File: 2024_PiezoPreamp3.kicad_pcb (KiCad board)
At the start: 4 copper layers, 71 x 36.8 mm, 91 parts, among them J101 6.3mm stereo, J102 6.3mm stereo, J201 DC IN 5.5/2.1mm, J401 Spring Contact, U101 OPA145, U102 OPA145, U201 ZXMP3A17E6TA, U301 BC847BS,115

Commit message: Schematic, PCB: moving DC ESD protection in front of the switch. Using one 22uF bulk decoupling cap where DC enters the board instead of two 10uF near opamps. Using 22uF instead of 10uF in opamp biasing to remove 10uF from BOM completely
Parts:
- removed the C203 at (158.9, 91.7)
- removed the C205 at (162.4, 83.0)
- removed C207: 10u, library:cap_CL21A106KAYNNNE
- added C201: 22u, library:cap_CL31A226KAHNNNE, F.Cu at (184.3, 83.5)
- added C204: 22u, library:cap_CL31A226KAHNNNE, F.Cu at (158.7, 91.2)
- moved D201 17.0 mm to (184.3, 88.2), turned to 90 degrees
- renumbered C201 to C202, C202 to C203, C204 to C205
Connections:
- D201 pad 2: /2-Power/DC_IN_ESD -> /2-Power/DC_IN_POS
- S201 pad 11: /2-Power/DC_IN_ESD -> /2-Power/RP_DRAIN
- U201 pad 1: /2-Power/DC_IN_ESD -> /2-Power/RP_DRAIN
- U201 pad 2: /2-Power/DC_IN_ESD -> /2-Power/RP_DRAIN
- U201 pad 5: /2-Power/DC_IN_ESD -> /2-Power/RP_DRAIN
- U201 pad 6: /2-Power/DC_IN_ESD -> /2-Power/RP_DRAIN
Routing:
- net /2-Power/DC_IN_ESD: track 30.3 -> 0.00 mm
- net /2-Power/RP_DRAIN: track 0.00 -> 22.8 mm
- net Vbias: track 24.8 -> 15.9 mm
- net GND: track 10.4 -> 9.11 mm, vias 27 -> 26
- net VS: track 53.3 -> 52.2 mm

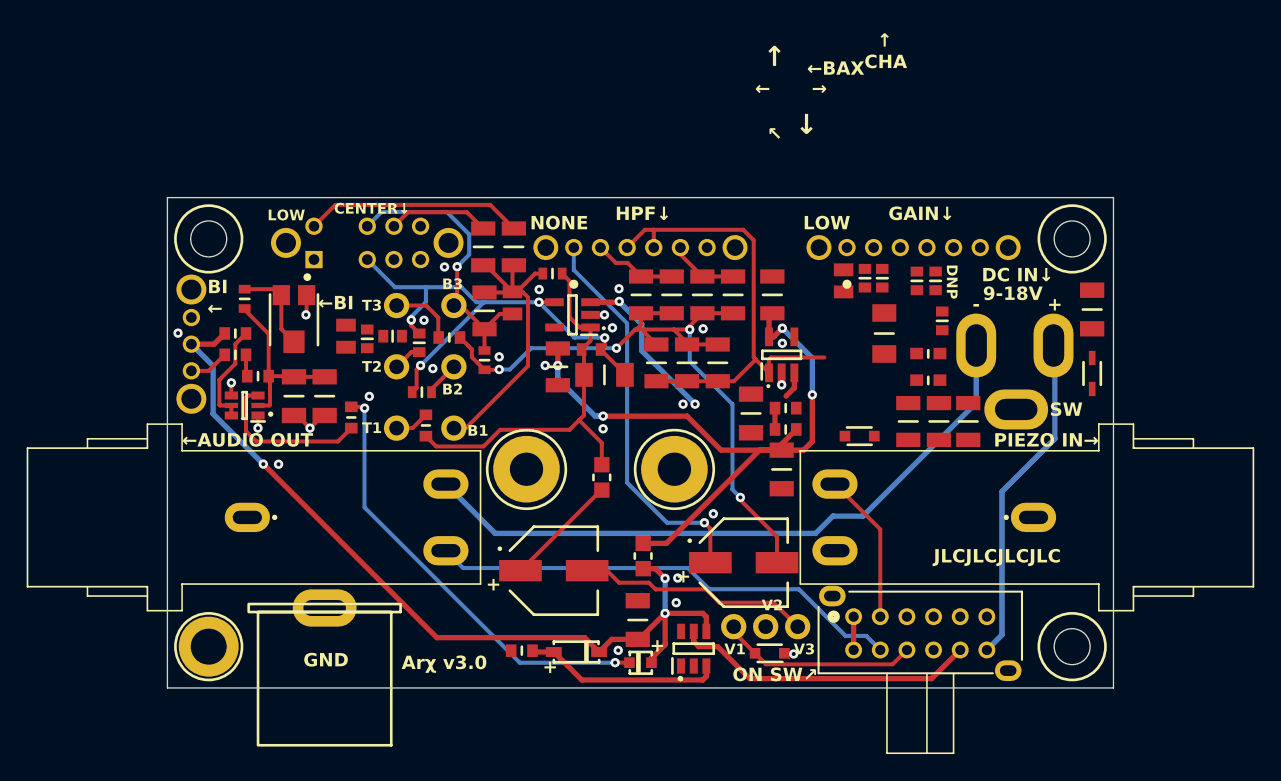
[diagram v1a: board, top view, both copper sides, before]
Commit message: PCB: changing power traces to 0.5mm width again. I have enough space and the inductance is lower
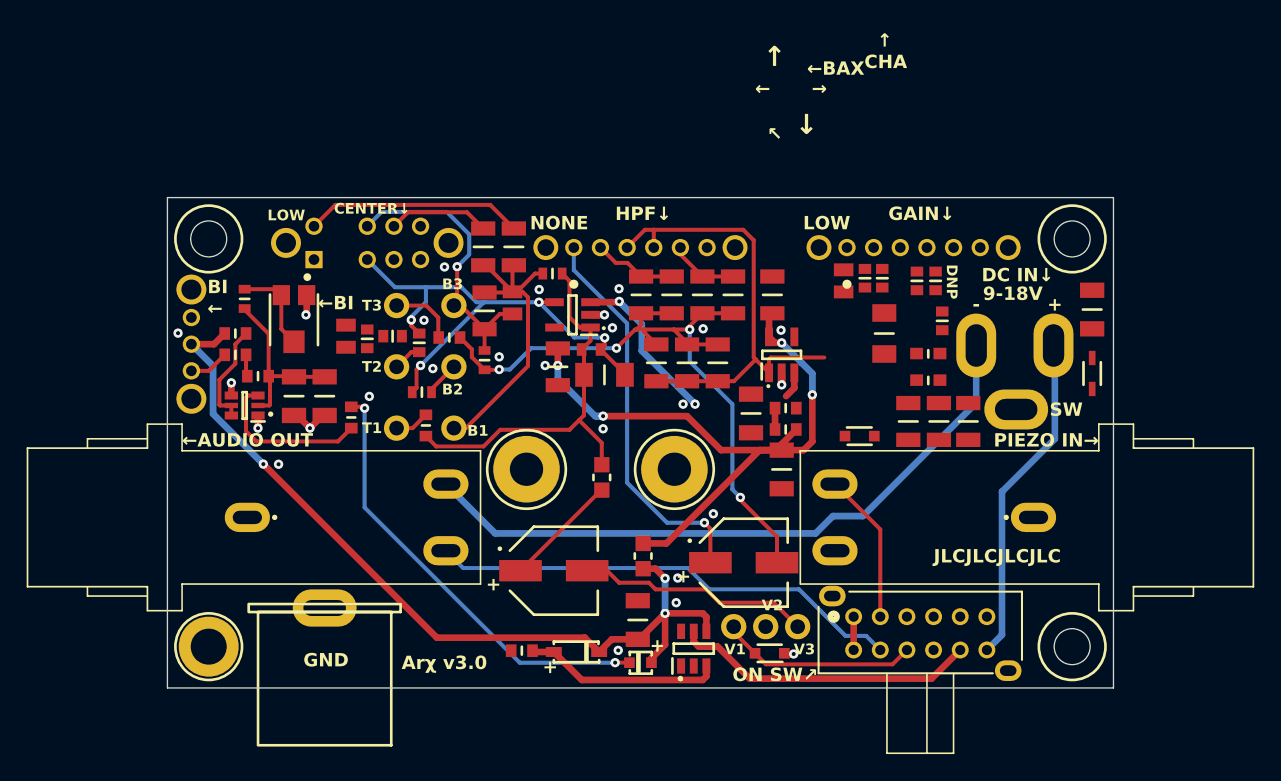
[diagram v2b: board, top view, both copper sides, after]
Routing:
- net VS: track 52.2 -> 51.0 mm

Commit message: PCB: enlarging all the pads that will be manually soldered
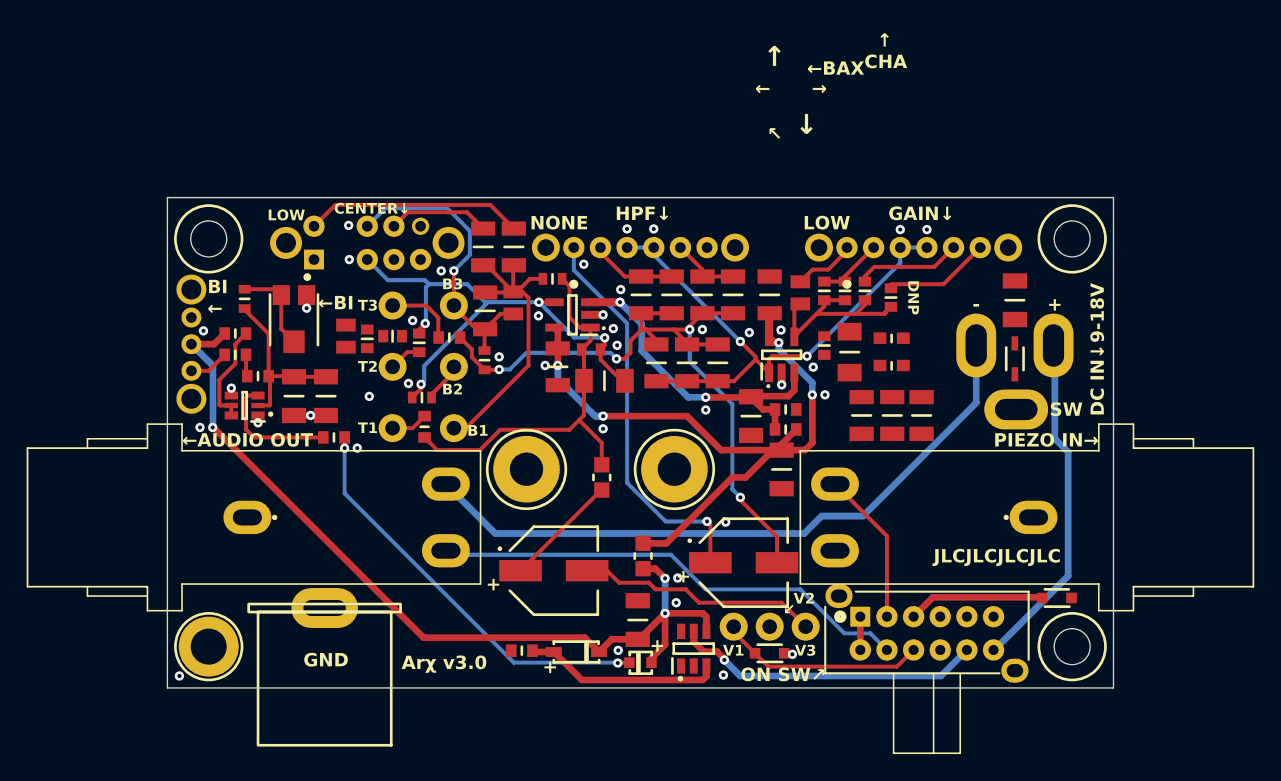
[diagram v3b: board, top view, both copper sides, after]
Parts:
- D202: value DDZ12B-7 -> SOD3716X145N
- S201: value EG4208A -> SWITCH12_EG4208A_EWI
- U201: value ZXMP3A17E6TA -> SOT95P285X140-6N
- moved D101 19.1 mm to (181.7, 105.1), turned to 180 degrees
- moved Cf101 9.04 mm to (164.2, 86.2)
- moved D201 5.90 mm to (178.5, 87.2)
- moved C201 5.84 mm to (178.5, 82.8)
- moved Cf105 3.97 mm to (167.2, 82.0)
- moved Cf106 3.58 mm to (169.2, 82.5)
- moved C101 3.53 mm to (169.3, 91.4)
- moved C102 3.53 mm to (171.5, 91.4)
- moved C103 3.53 mm to (167.0, 91.4)
- moved Cf102 3.37 mm to (162.4, 82.2)
- moved Cf104 3.19 mm to (164.2, 82.0)
- moved R101 2.98 mm to (169.2, 85.6)
- moved R102 2.96 mm to (169.2, 87.7)
- moved Cf103 2.96 mm to (165.8, 82.0)
- moved Rf101 2.95 mm to (166.1, 86.7)
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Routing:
- net /1-ChargeAmpAndEQ/CH_A_INV: track 0.00 -> 14.7 mm
- net PIEZO_ESD: track 0.00 -> 10.3 mm
- net Vbias: track 15.9 -> 24.7 mm
- net /1-ChargeAmpAndEQ/G_SW_5: track 0.00 -> 7.94 mm
- net /1-ChargeAmpAndEQ/G_SW_6: track 0.00 -> 7.84 mm
- net /1-ChargeAmpAndEQ/G_SW_1: track 0.00 -> 5.06 mm
- net /1-ChargeAmpAndEQ/G_SW_2: track 0.00 -> 4.96 mm
- net /1-ChargeAmpAndEQ/CH_A_OUT: track 35.5 -> 40.1 mm, vias 0 -> 3
- net /3-BatteryIndicator/BI_C2: track 12.1 -> 9.41 mm
- net /3-BatteryIndicator/LED_K: track 33.2 -> 30.9 mm
- net GND: track 9.11 -> 6.89 mm, vias 26 -> 39
- net VS: track 51.0 -> 52.6 mm
- net /1-ChargeAmpAndEQ/BAX_IN: track 53.0 -> 54.2 mm
- net /1-ChargeAmpAndEQ/BAX_A_INV: track 38.4 -> 39.4 mm
- net /2-Power/DC_IN_POS: track 25.0 -> 25.7 mm
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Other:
- board text added: "↙"

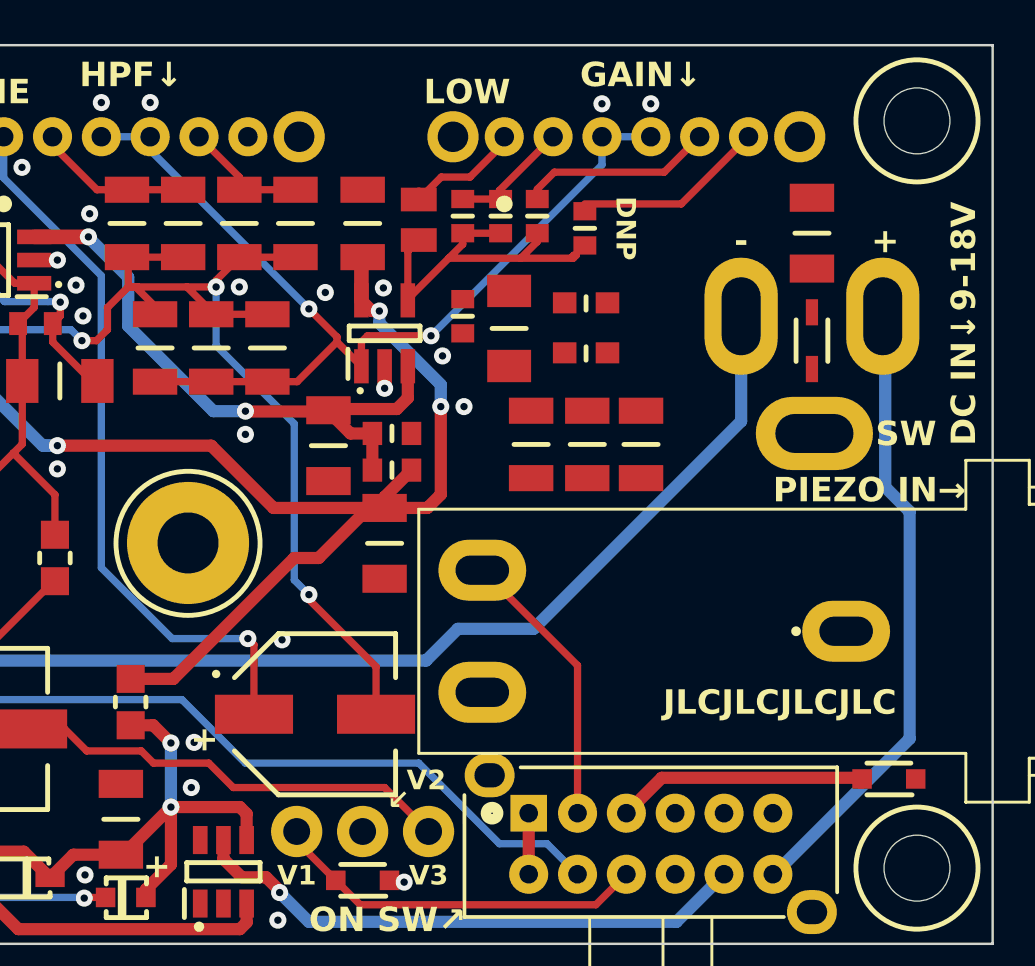
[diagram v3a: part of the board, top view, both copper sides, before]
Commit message: Using larger footprint for DNP feedback cap; small improvements
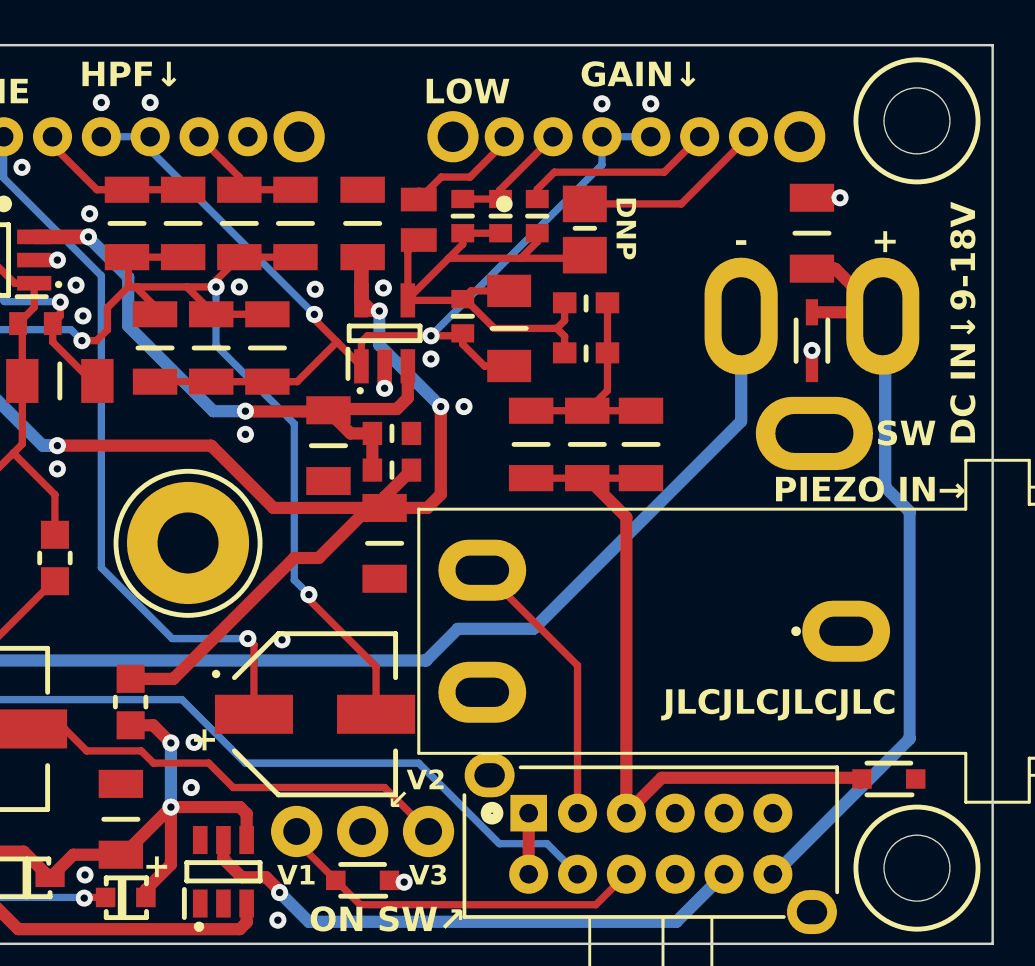
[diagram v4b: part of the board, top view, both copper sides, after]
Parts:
- Cf106: footprint library:GRM1885C1H102JA01D -> library:cap_SMD_DNP
- D202: value SOD3716X145N -> DDZ12B-7
- S201: value SWITCH12_EG4208A_EWI -> EG4208A
- U201: value SOT95P285X140-6N -> ZXMP3A17E6TA
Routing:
- net PIEZO_ESD: track 10.3 -> 29.2 mm
- net /1-ChargeAmpAndEQ/CH_A_INV: track 14.7 -> 25.6 mm
- net /1-ChargeAmpAndEQ/CIN_RIN: track 0.00 -> 9.26 mm
- net /2-Power/DC_IN_POS: track 25.7 -> 32.3 mm
- net /1-ChargeAmpAndEQ/CH_A_OUT: track 40.1 -> 44.2 mm, vias 3 -> 2
- net GND: track 6.89 -> 8.80 mm, vias 39 -> 42

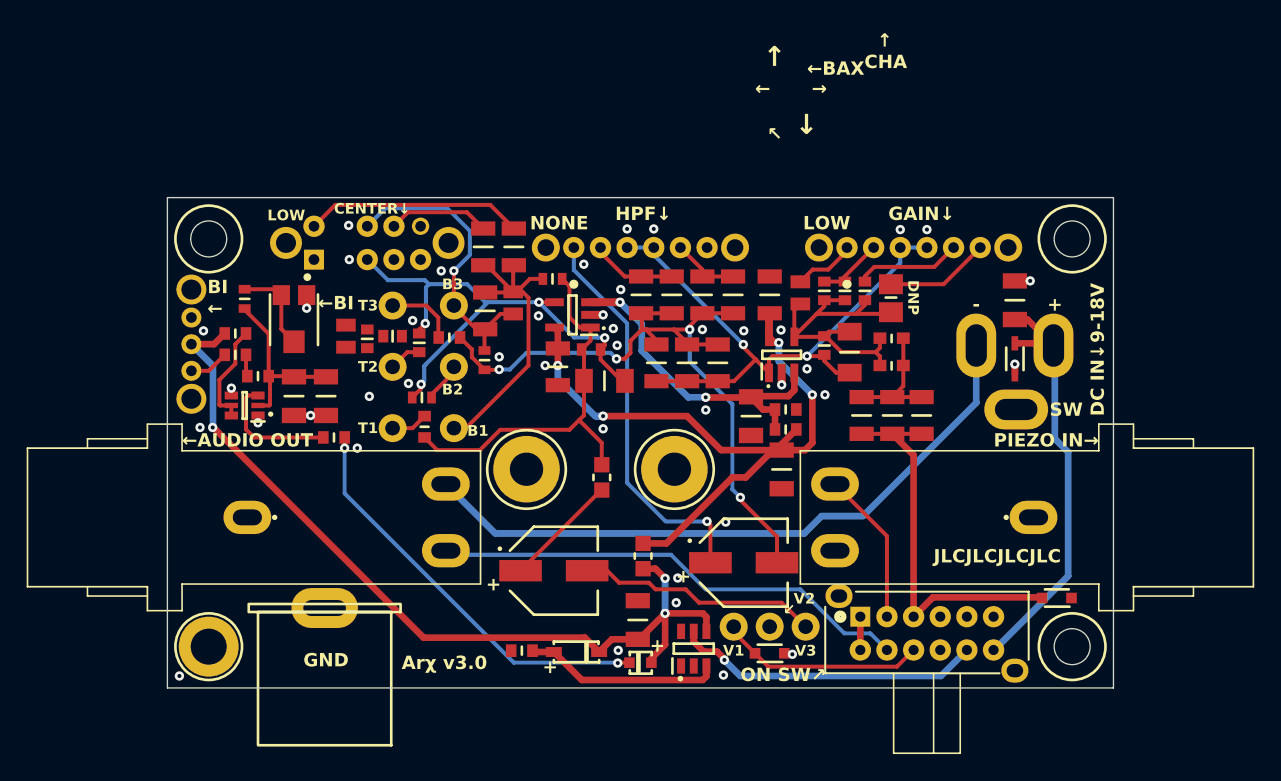
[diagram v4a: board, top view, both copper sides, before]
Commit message: PCB: finishing layout & routing, improving silkscreen everywhere, checking rules
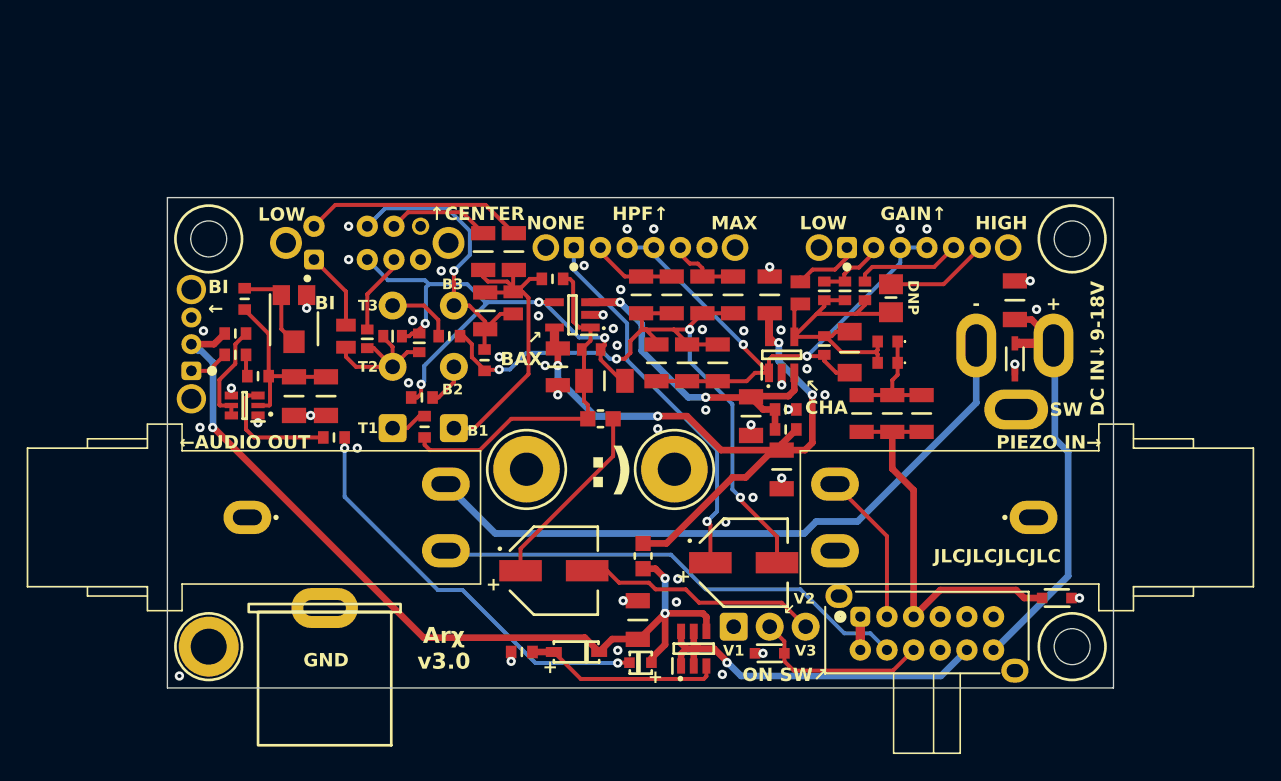
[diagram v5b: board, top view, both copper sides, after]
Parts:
- C205, C206, Cb103, Chp107: footprint library:GRM31C5C2A104JA01L -> library:GRM31C5C1H104JA01L
- H101, H104, H107: footprint library:FreePad_1.1mm_2.0mm -> library:FreePad_1.1mm_2.1mm_rect
- H102, H103, H105, H106, H108, H109: footprint library:FreePad_1.1mm_2.0mm -> library:FreePad_1.1mm_2.1mm
- R101, R102: footprint library:RT0603BRE07150RL_UL-M -> library:ERA-3AEB151V
- R103, R303, Rb101, Rb102: footprint library:ERA-3AEB392V -> library:RT0603FRE073K9L
- R203, R204, R301, R302, R304: footprint library:RT0603BRD0747KL -> library:RT0603FRD0747KL
- moved R105 4.40 mm to (147.4, 91.7), turned to 180 degrees
- moved H107 2.70 mm to (157.4, 107.2)
- moved H108 2.70 mm to (160.1, 107.2)
- moved R101 0.39 mm to (168.9, 85.8)
- moved R102 0.36 mm to (168.9, 87.5)
- moved Cb103 0.35 mm to (140.9, 79.1)
- moved Cb104 0.35 mm to (138.6, 79.1)
- moved C101 0.15 mm to (169.3, 91.2)
- moved C102 0.15 mm to (171.5, 91.2)
- moved C103 0.15 mm to (167.0, 91.2)
- moved R201 0.10 mm to (141.5, 109.2)
- moved Rt101 0.10 mm to (136.1, 85.5)
- turned D102 to 0 degrees
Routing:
- net /1-ChargeAmpAndEQ/TREB_2: track 2.46 -> 12.1 mm
- net GND: track 8.80 -> 15.2 mm, vias 42 -> 51
- net /1-ChargeAmpAndEQ/C_SW_2: track 0.00 -> 6.08 mm
- net /1-ChargeAmpAndEQ/C_SW_1: track 0.00 -> 5.91 mm
- net /1-ChargeAmpAndEQ/ROUT_COUT: track 8.61 -> 14.3 mm
- net /2-Power/RP_DRAIN: track 23.3 -> 28.9 mm
- net VS: track 52.6 -> 56.3 mm
- net /1-ChargeAmpAndEQ/BAX_A_OUT: track 29.4 -> 27.1 mm
- net AUDIO_ESD: track 15.5 -> 13.7 mm
- net /1-ChargeAmpAndEQ/BAX_A_INV: track 39.4 -> 41.0 mm
- net /1-ChargeAmpAndEQ/HPF_SW_1: track 29.7 -> 28.5 mm
- net /1-ChargeAmpAndEQ/BASS_1: track 23.8 -> 24.7 mm
- net /1-ChargeAmpAndEQ/CH_A_INV: track 25.6 -> 25.0 mm
- net PIEZO_ESD: track 29.2 -> 29.8 mm
- net /1-ChargeAmpAndEQ/CH_A_OUT: track 44.2 -> 44.8 mm
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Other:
- board text added: ":)"
- board text added: "A OUT"
- board text added: "BI"
- board text added: "BI SW↑"
- board text added: "DC -"
- board text added: "GAIN↑"
- board text added: "HIGH"
- board text added: "HPF↑"
- board text added: "MAX"
- board text added: "PIEZO IN"
- board text added: "Piezo Preamp v3.0 03/2024 Arx arx.wtf"
- board text added: "RD"
- board text added: "←ON/OFF SW"
- board text added: "↑CENTER"
- board text added: "↖ CHA"
- board text added: "↗ BAX"
- board text removed: "BI SW"
- board text removed: "CENTER↓"
- board text removed: "DE"
- board text removed: "GAIN↓"
- board text removed: "HPF↓"
- board text removed: "ON/OFF SW"
- board text removed: "Piezo Preamp v3.0 03/2024 Arχ arx.wtf"
- board text removed: "←"
- board text removed: "←BAX"
- board text removed: "←BI"
- board text removed: "↑"
- board text removed: "↑ CHA"
- board text removed: "↓"
- board text removed: "↖"
